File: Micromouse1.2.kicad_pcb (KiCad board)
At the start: 2 copper layers, 70.4 x 87.9 mm, 123 parts, among them J1 USB_B, P1 CONN_01X4, Q1 Q_NMOS_DGS, Q2 Q_NMOS_DGS, Q3 Q_NMOS_DGS, Q4 Q_NMOS_DGS, Q5 Q_NMOS_DGS, Q6 Q_NMOS_DGS, U1 BAT54C, U10 CONN_02X03, U14 ferrite, U15 LMZ21701, U16 JST_Connector, U17 Switch_micromouse, U18 LMZ21701, U19 splitter, U2 DRV8833, U20 TPD3S014, U21 MKL02Z32VFG4, U22 LP38691, U23 MK66FX1M0, U24 Test_Point, U25 Test_Point, U26 Test_Point, U27 Test_Point, U28 Test_Point, U29 Test_Point, U3 ferrite, U30 Test_Point, U31 MPU-6500, U32 Motor_mount, U4 TPS61222DCK, U5 ferrite, U6 BAT54C, U7 Test_Point, U9 CONN_02X03, Y1 Crystal_16MHz, Y2 32.768MHz

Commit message: Rev 1.0 done
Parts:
- added C3: 0.01uF, micromouse:C_0603, F.Cu at (118.5, 102.9)
- added R32: R, Capacitors_SMD:C_0402, F.Cu at (102.2, 106.2)
- added R33: R, Capacitors_SMD:C_0402, F.Cu at (101.7, 108.9)
- added R34: R, Capacitors_SMD:C_0402, F.Cu at (135.7, 111.9)
- added R35: R, Capacitors_SMD:C_0402, F.Cu at (136.8, 111.9)
- added R36: R, Capacitors_SMD:C_0402, F.Cu at (100.6, 111.5)
- added R41: R, Capacitors_SMD:C_0402, F.Cu at (101.7, 111.5)
- added R42: R, Capacitors_SMD:C_0402, F.Cu at (135.9, 108.7)
- added R43: R, Capacitors_SMD:C_0402, F.Cu at (137.0, 108.7)
- C10, C13: value 22uF -> 10uF
- C35: value C -> 2.2uF
- D1, D2, D3, D4, D5, D6: value D_Photo -> ~
- D10, D11, D12, D13, D8, D9: value IRL81A -> ~
- R25: value 383k -> 180k; footprint micromouse:R_0402 -> micromouse:R_0603
- R27: value 1.21M -> 562k
- R3: footprint Capacitors_SMD:C_0402 -> micromouse:R_0402
- U1: footprint PMEG4010_DIODE -> micromouse:PMEG4010_DIODE
- U14, U5: value ferrite -> 600
- U3: value ferrite -> 120
- U32: footprint Motor_mount -> micromouse:Motor_mount
- moved P1 88.4 mm to (111.3, 80.0)
- moved U32 80.0 mm to (118.9, 85.9)
- moved U17 61.4 mm to (107.9, 97.2)
- moved U1 9.35 mm to (122.7, 70.9)
- moved C17 8.97 mm to (120.0, 71.4)
- moved Q6 8.28 mm to (146.9, 51.2), turned to 174.7 degrees
- moved R37 7.93 mm to (127.6, 68.7)
- moved R38 7.85 mm to (127.4, 67.2)
- moved U19 5.16 mm to (106.8, 95.6)
- moved R20 5.01 mm to (146.7, 53.8), turned to 264.7 degrees
- moved U21 4.08 mm to (121.8, 63.4)
- moved s1 3.93 mm to (122.5, 67.2)
- moved Q4 3.42 mm to (126.8, 34.5), turned to 328 degrees
- moved C5 2.94 mm to (85.5, 56.1), turned to 94.3 degrees
- moved Q5 2.72 mm to (137.0, 38.3), turned to 125 degrees
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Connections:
- C10 pad 2: Net-(C10-Pad2) -> GNDD
- C22 pad 1: Net-(C22-Pad1) -> MCUv
- C23 pad 1: Net-(C22-Pad1) -> MCUv
- C25 pad 1: Net-(C22-Pad1) -> MCUv
- C27 pad 1: Net-(C22-Pad1) -> MCUv
- C29 pad 1: Net-(C22-Pad1) -> MCUv
- C34 pad 1: 3.3V -> MCUv
- P1 pad 4: 5V -> MCUv
- Q1 pad 2: L_EMITTER -> LF_EMITTER
- Q2 pad 2: RD_EMITTER -> L_EMITTER
- Q3 pad 2: RF_EMITTER -> LD_EMITTER
- Q4 pad 2: LF_EMITTER -> RD_EMITTER
- Q6 pad 2: LD_EMITTER -> RF_EMITTER
- U1 pad 1: Net-(C22-Pad1) -> MCUv
- U1 pad 2: Net-(C22-Pad1) -> MCUv
- U10 pad 1: L_CH_A -> Net-(R34-Pad1)
- U10 pad 2: L_CH_B -> Net-(R42-Pad1)
- U14 pad 1: Net-(C22-Pad1) -> MCUv
- U15 pad 5: Net-(C10-Pad2) -> GNDD
- U2 pad 1: Net-(R30-Pad1) -> GNDD
- U2 pad 4: Net-(R30-Pad1) -> GNDD
- U21 pad 1: Net-(C22-Pad1) -> MCUv
- U22 pad 4: Net-(C22-Pad1) -> MCUv
- U22 pad 5: Net-(C22-Pad1) -> MCUv
- U23 pad A11: Net-(U23-PadA11) -> TX
- U23 pad A12: Net-(U23-PadA12) -> INT
- U23 pad A5: R_CH_B -> R_CH_A
- U23 pad A9: Net-(U23-PadA9) -> RX
- U23 pad B1: Net-(U23-PadB1) -> L_CH_B
- U23 pad B12: Net-(U23-PadB12) -> FSYNC
- U23 pad B4: Net-(U23-PadB4) -> R_CH_B
- U23 pad C1: Net-(U23-PadC1) -> L_CH_A
- U23 pad E5: Net-(C22-Pad1) -> MCUv
- U23 pad E6: Net-(C22-Pad1) -> MCUv
- U23 pad E7: Net-(C22-Pad1) -> MCUv
- U23 pad E8: Net-(C22-Pad1) -> MCUv
- U23 pad F5: Net-(C22-Pad1) -> MCUv
- U23 pad F8: Net-(C22-Pad1) -> MCUv
- U23 pad G1: Net-(C22-Pad1) -> MCUv
- U23 pad H10: Net-(U23-PadH10) -> RF_RECEIVER
- U23 pad H11: Net-(U23-PadH11) -> L_EMITTER
- U23 pad H12: Net-(U23-PadH12) -> LF_EMITTER
- U23 pad H9: Net-(U23-PadH9) -> R_RECEIVER
- U23 pad J9: Net-(U23-PadJ9) -> LD_EMITTER
- U23 pad K10: Net-(U23-PadK10) -> R_EMITTER
- U23 pad K11: Net-(U23-PadK11) -> RF_EMITTER
- U23 pad K9: Net-(U23-PadK9) -> RD_EMITTER
- U23 pad L3: RF_RECEIVER -> Net-(U23-PadL3)
- U23 pad L4: R_RECEIVER -> Net-(U23-PadL4)
- U31 pad 13: 3.3V -> MCUv
- U9 pad 1: R_CH_A -> Net-(R33-Pad1)
- U9 pad 2: R_CH_B -> Net-(R41-Pad1)
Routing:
- net R_EMITTER: track 0.00 -> 78.4 mm, vias 0 -> 2
- net RD_EMITTER: track 0.00 -> 61.3 mm, vias 0 -> 2
- net RF_EMITTER: track 0.00 -> 60.9 mm
- net MCUv: track 0.00 -> 55.4 mm, vias 0 -> 4
- net GNDD: track 25.7 -> 79.0 mm, vias 6 -> 14
- net GNDA: track 7.12 -> 60.2 mm, vias 6 -> 7
- net (no net): track 52.9 -> 0.97 mm
- net L_CH_A: track 0.00 -> 50.1 mm
- net LD_EMITTER: track 0.00 -> 49.9 mm, vias 0 -> 2
- net L_CH_B: track 0.00 -> 49.2 mm
- net R_CH_B: track 0.00 -> 46.6 mm
- net R_CH_A: track 0.00 -> 42.9 mm
- net Net-(U23-PadA12): track 42.7 -> 0.00 mm, vias 2 -> 0
- net LD_RECEIVER: track 18.7 -> 61.2 mm, vias 2 -> 1
- net Net-(U23-PadA11): track 41.6 -> 0.00 mm, vias 2 -> 0
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- added copper zone on F.Cu, net GNDA
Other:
- outline, holes or cut-outs redrawn

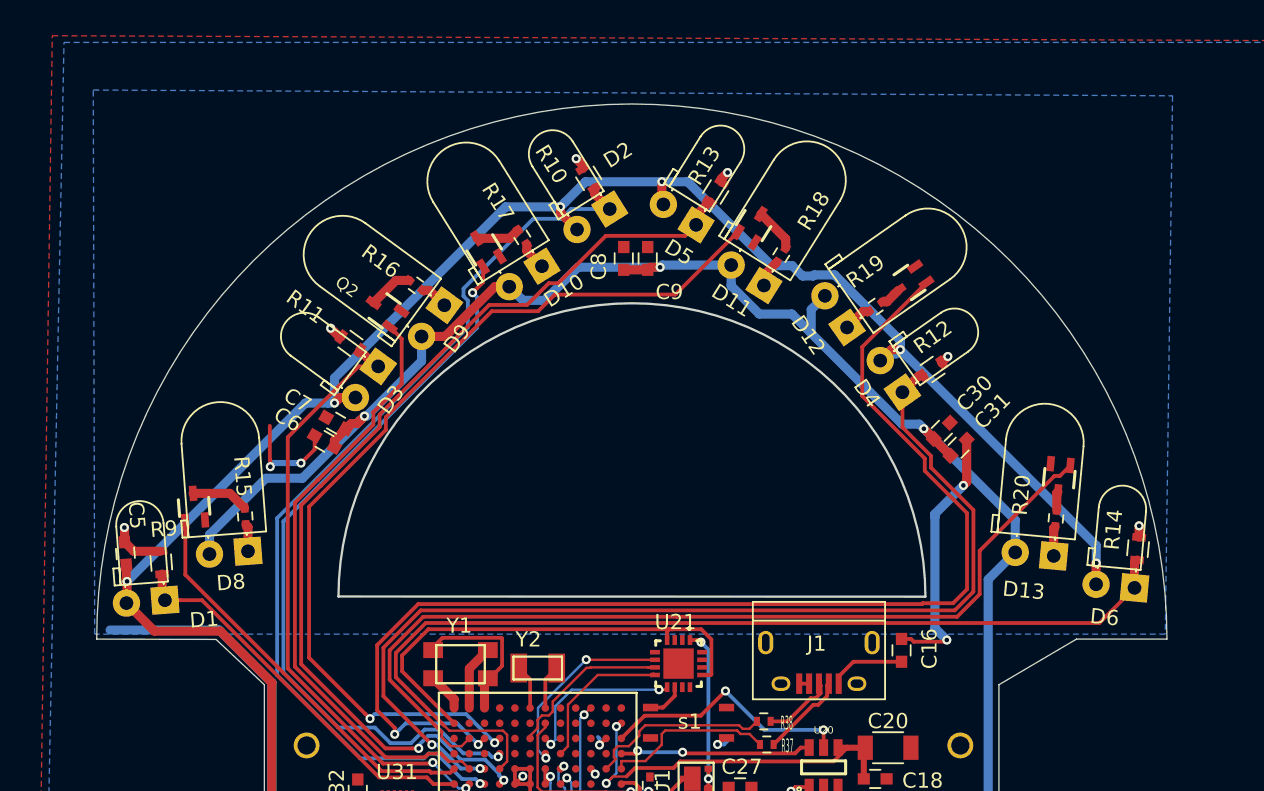
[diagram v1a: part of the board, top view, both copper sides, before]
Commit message: added isolated island underneath the 16Mhz Crystal
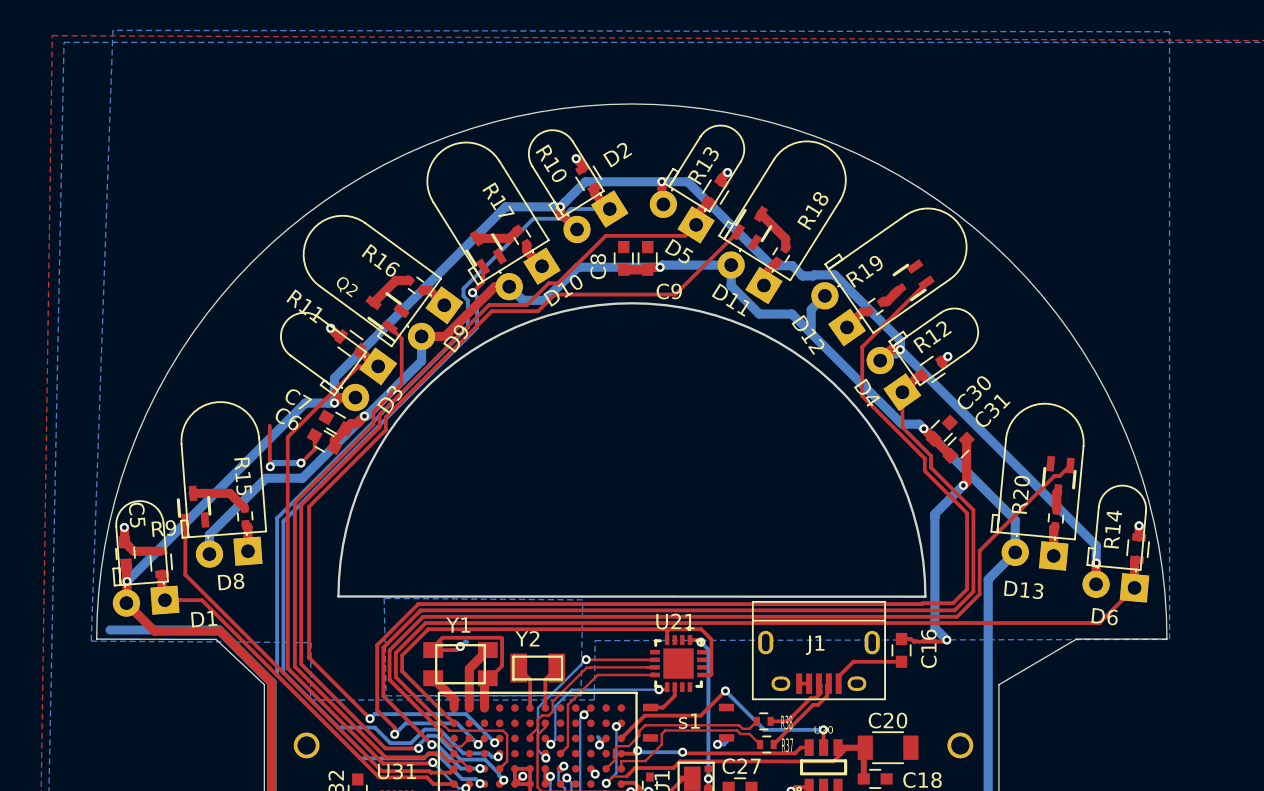
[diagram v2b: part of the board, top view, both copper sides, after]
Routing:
- net GNDD: track 79.0 -> 81.4 mm, vias 14 -> 15
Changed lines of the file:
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@@
     (thickness 1.6)
     (drawings 18)
-    (tracks 1182)
+    (tracks 1187)
     (zones 0)
     (modules 132)
@@
   (segment (start 85.396166 54.420366) (end 85.3824 54.4066) (width 0.6) (layer F.Cu) (net 3))
   (via (at 85.3824 54.4066) (size 0.6) (drill 0.3) (layers F.Cu B.Cu) (net 3))
+  (segment (start 107.4824 62.2366) (end 107.782399 61.936601) (width 0.25) (layer B.Cu) (net 5))
+  (segment (start 107.782399 61.936601) (end 107.942399 61.936601) (width 0.25) (layer B.Cu) (net 5))
+  (segment (start 105.6928 62.4696) (end 107.2494 62.4696) (width 0.25) (layer F.Cu) (net 5))
+  (segment (start 107.2494 62.4696) (end 107.4824 62.2366) (width 0.25) (layer F.Cu) (net 5))
+  (via (at 107.4824 62.2366) (size 0.6) (drill 0.3) (layers F.Cu B.Cu) (net 5))
   (segment (start 104.176813 75.701342) (end 104.376261 75.477361) (width 0.25) (layer F.Cu) (net 5))
   (segment (start 104.17176 76.40186) (end 104.17176 75.706395) (width 0.25) (layer F.Cu) (net 5))
@@
     )
   )
-  (zone (net 3) (net_name GNDA) (layer B.Cu) (hatch none 0.508)
+  (zone (net 3) (net_name GNDA) (layer F.Cu) (hatch none 0.508)
+    (priority 36)
+    (connect_pads yes (clearance 0.02))
+    (min_thickness 0.0254)
+    (fill yes (mode segment) (arc_segments 16) (thermal_gap 0.508) (thermal_bridge_width 0.508))
+    (polygon
+      (pts
+        (xy 106.5224 95.9666) (xy 105.1124 95.9666) (xy 105.1024 94.6066) (xy 106.5124 94.6066)
+      )
+    )
+  )
+  (zone (net 3) (net_name GNDA) (layer B.Cu) (hatch edge 0.508)
     (priority 36)
     (connect_pads yes (clearance 0.02))
@@
     (polygon
       (pts
-        (xy 83.3374 25.6286) (xy 154.3304 26.0096) (xy 153.8524 61.4166) (xy 83.4309 61.4166)
+        (xy 83.2024 61.8766) (xy 97.6724 61.9766) (xy 97.6224 65.7566) (xy 116.2924 65.7466) (xy 116.3524 61.8466)
+        (xy 154.1324 61.7666) (xy 154.1324 21.7966) (xy 84.6324 21.7066)
       )
     )
   )
-  (zone (net 3) (net_name GNDA) (layer F.Cu) (hatch none 0.508)
+  (zone (net 5) (net_name GNDD) (layer B.Cu) (hatch edge 0.508)
     (priority 36)
     (connect_pads yes (clearance 0.02))
-    (min_thickness 0.0254)
-    (fill yes (mode segment) (arc_segments 16) (thermal_gap 0.508) (thermal_bridge_width 0.508))
+    (min_thickness 0.254)
+    (fill yes (arc_segments 16) (thermal_gap 0.508) (thermal_bridge_width 0.508))
     (polygon
       (pts
-        (xy 106.5224 95.9666) (xy 105.1124 95.9666) (xy 105.1024 94.6066) (xy 106.5124 94.6066)
+        (xy 104.6124 65.4666) (xy 115.4224 65.4566) (xy 115.5324 59.1666) (xy 102.4724 59.0666) (xy 102.6024 65.4766)
+        (xy 115.4224 65.4566)
       )
     )
